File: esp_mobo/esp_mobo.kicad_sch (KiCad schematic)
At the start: 4 parts, among them J1 JST XH Power in, U1 ESP32-DevKitC, U2 74AHCT125

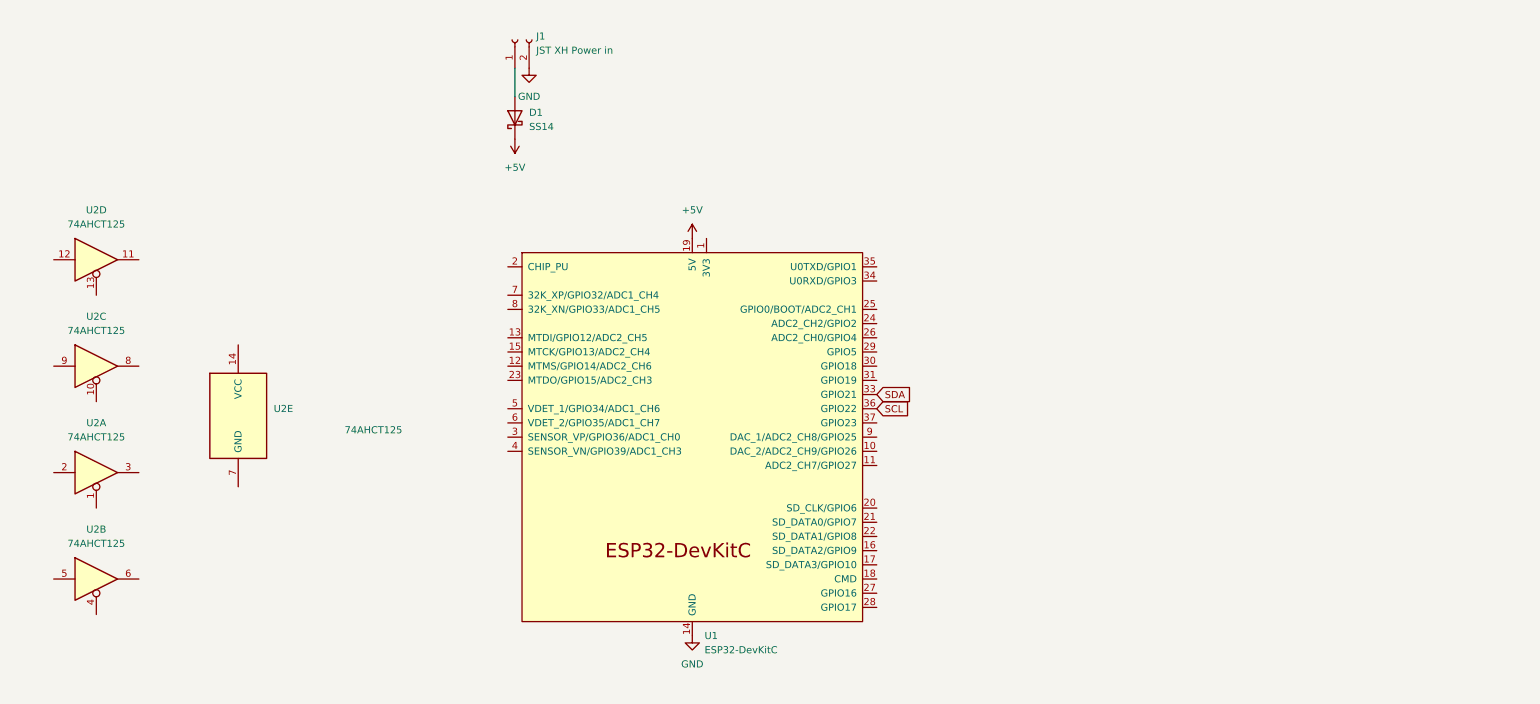
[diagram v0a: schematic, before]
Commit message: add submodule for testing
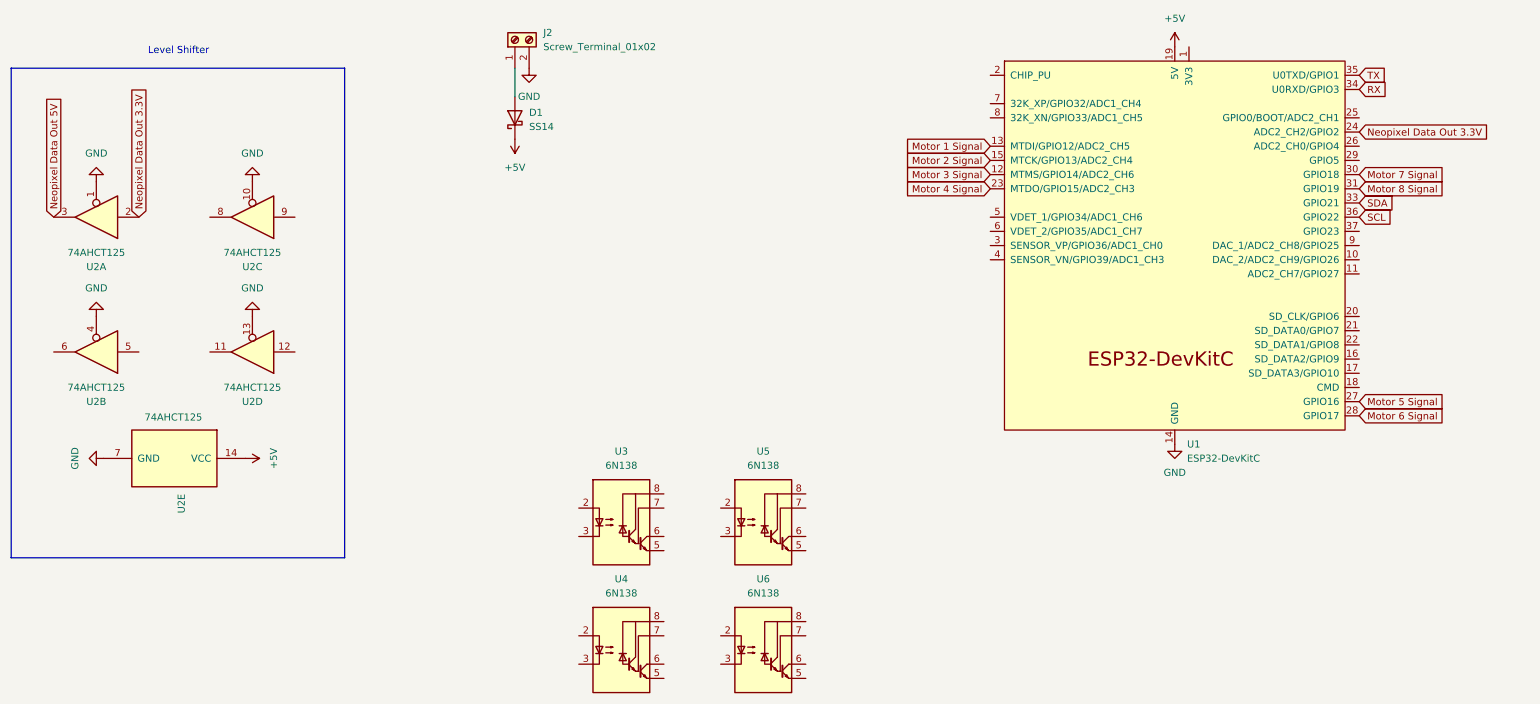
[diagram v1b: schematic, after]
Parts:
- removed J1: JST XH Power in, Connector_JST:JST_XH_B2B-XH-AM_1x02_P2.50mm_Vertical, symbol Connector:Conn_01x02_Socket
- added J2: Screw_Terminal_01x02, TerminalBlock_TE-Connectivity:TerminalBlock_TE_282834-2_1x02_P2.54mm_Horizontal, symbol Connector:Screw_Terminal_01x02
- added U3, U4, U5, U6: 6N138, symbol Isolator:6N138
- U2: footprint (none) -> Package_DIP:DIP-14_W7.62mm
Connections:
- net +5V: now also U2.14 (VCC)
- net GND: now also U2.1, U2.10, U2.13, U2.4, U2.7 (GND), J2.2 (Pin_2)
- net at D1.2 (A): now also J2.1 (Pin_1)
- net Motor 3 Signal: now reaches U1.12 (MTMS/GPIO14/ADC2_CH6)
- net Motor 1 Signal: now reaches U1.13 (MTDI/GPIO12/ADC2_CH5)
- net Motor 2 Signal: now reaches U1.15 (MTCK/GPIO13/ADC2_CH4)
- net Motor 4 Signal: now reaches U1.23 (MTDO/GPIO15/ADC2_CH3)
- net Neopixel Data Out 3.3V: now reaches U1.24 (ADC2_CH2/GPIO2)
- net Neopixel Data Out 3.3V: now also U2.2
- net Motor 5 Signal: now reaches U1.27 (GPIO16)
- net Motor 6 Signal: now reaches U1.28 (GPIO17)
- net Motor 7 Signal: now reaches U1.30 (GPIO18)
- net Motor 8 Signal: now reaches U1.31 (GPIO19)
- net RX: now reaches U1.34 (U0RXD/GPIO3)
- net TX: now reaches U1.35 (U0TXD/GPIO1)
- net Neopixel Data Out 5V: now reaches U2.3
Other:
- note added: "Level Shifter"
- moved on the sheet: U1, U2A, U2B, U2C, U2D, U2E

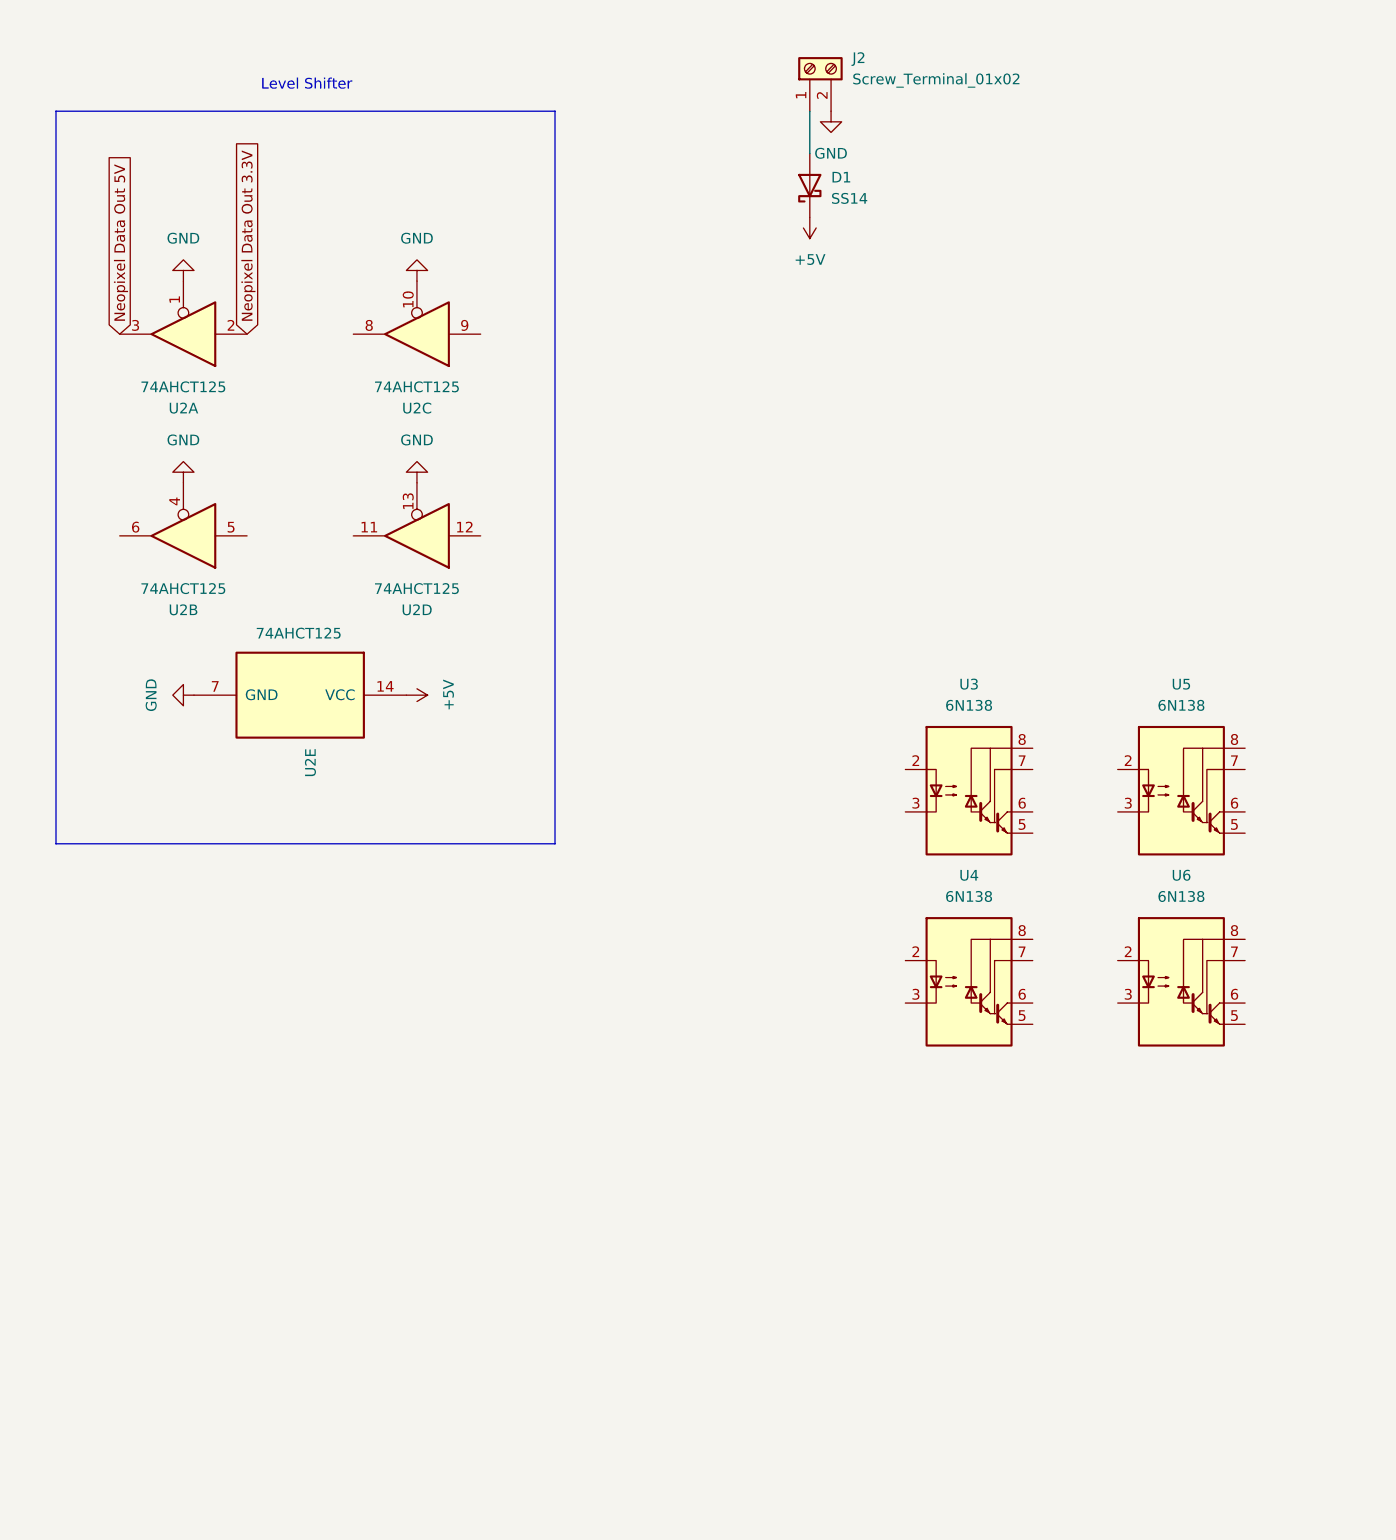
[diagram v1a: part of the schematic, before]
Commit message: Update ESC Mobo with OptoCOuplers and improved circuit
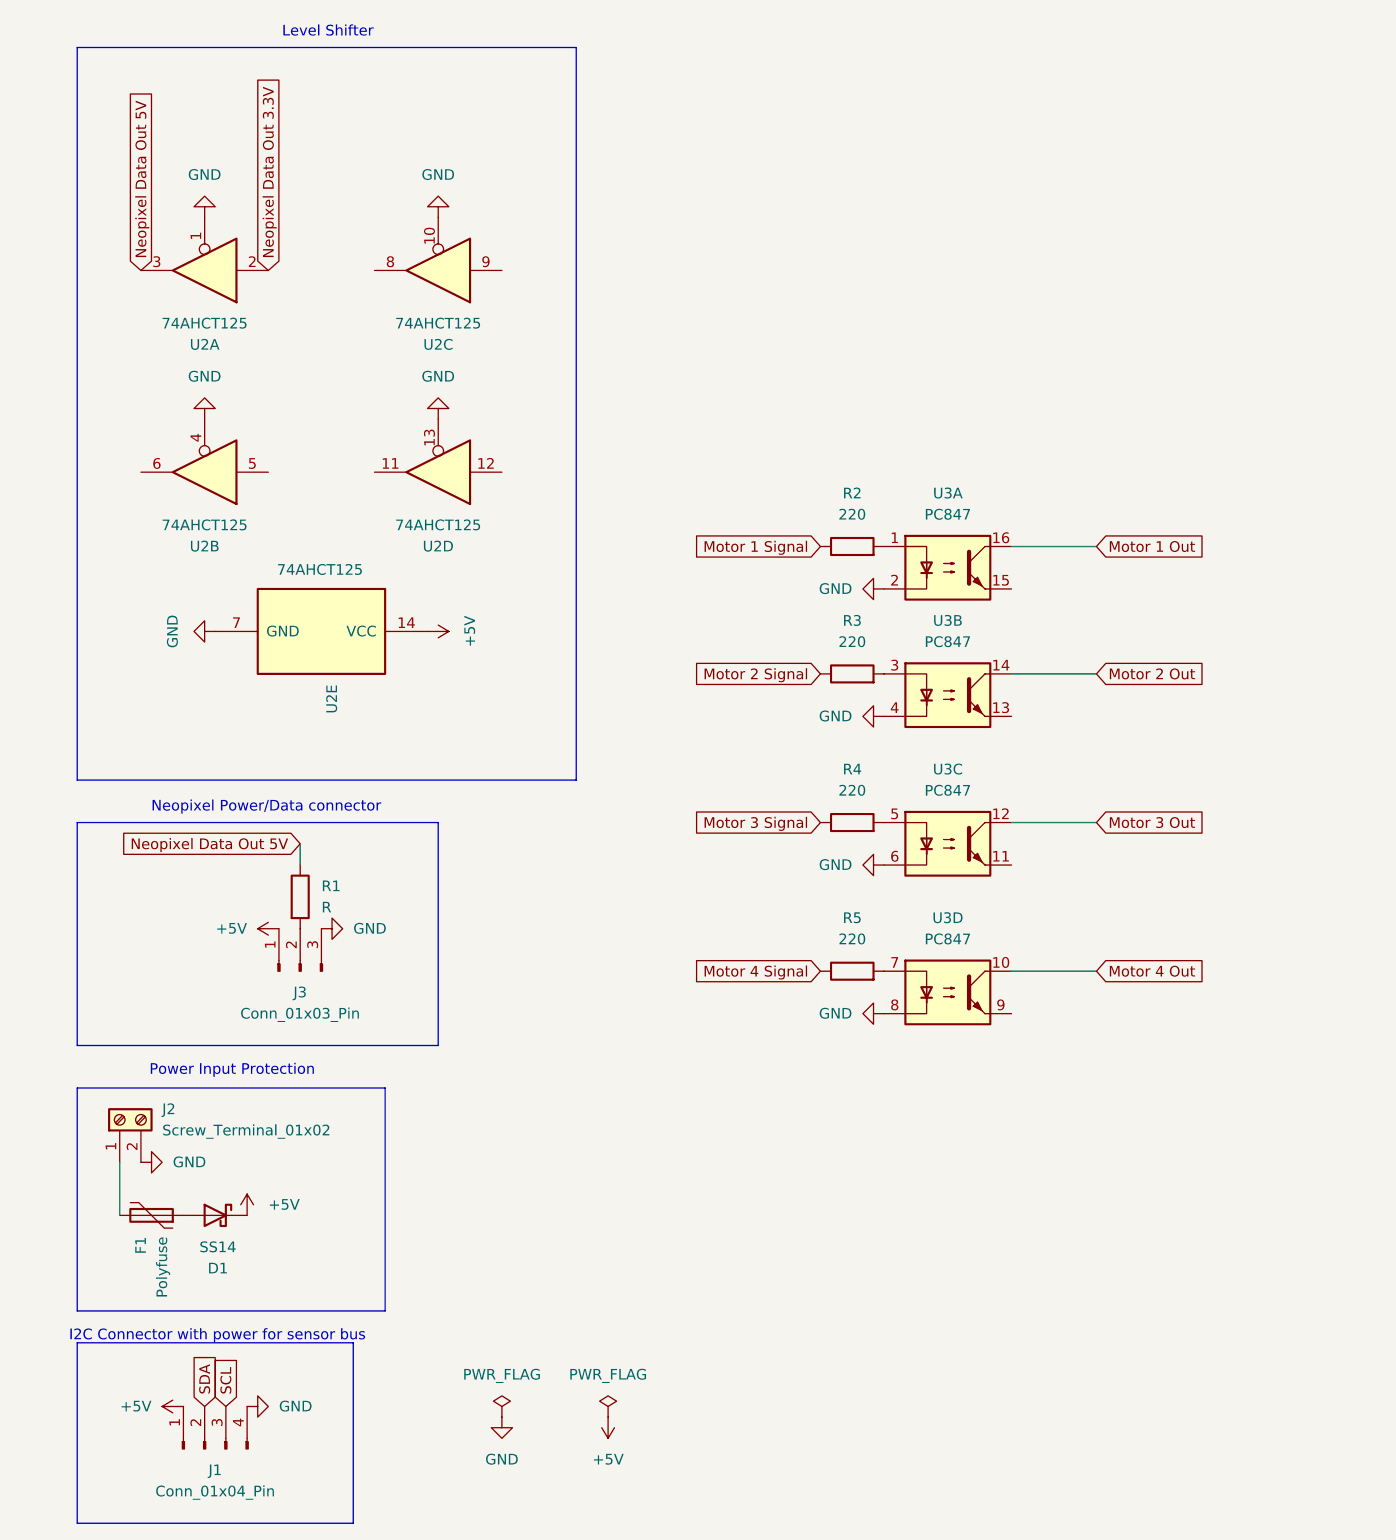
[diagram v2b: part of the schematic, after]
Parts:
- removed U3, U4, U5, U6: 6N138, symbol Isolator:6N138
- added F1: Polyfuse, symbol Device:Polyfuse
- added J1: Conn_01x04_Pin, Connector_JST:JST_XH_B4B-XH-AM_1x04_P2.50mm_Vertical, symbol Connector:Conn_01x04_Pin
- added J3: Conn_01x03_Pin, symbol Connector:Conn_01x03_Pin
- added R1: R, symbol Device:R
- added R2, R3, R4, R5: 220, Resistor_SMD:R_0603_1608Metric_Pad0.98x0.95mm_HandSolder, symbol Device:R
- added U3: PC847, Package_DIP:DIP-16_W7.62mm, symbol Isolator:PC847
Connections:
- net +5V: now also J1.1 (Pin_1), J3.1 (Pin_1)
- net GND: now also J1.4 (Pin_4), J3.3 (Pin_3), U3.2, U3.4, U3.6, U3.8
- net Motor 1 Signal: now also R2.1
- net Motor 2 Signal: now also R3.1
- net Motor 3 Signal: now also R4.1
- net Motor 4 Signal: now also R5.1
- net Neopixel Data Out 5V: now also R1.1
- net SCL: now also J1.3 (Pin_3)
- net SDA: now also J1.2 (Pin_2)
- net at J2.1 (Pin_1): now also F1.2; no longer D1.2 (A)
- new net: J3.2 (Pin_2), R1.2
- new net: R2.2, U3.1
- new net: D1.2 (A), F1.1
- new net: R3.2, U3.3
- new net: R5.2, U3.7
- new net: R4.2, U3.5
- new net Motor 1 Out: U3.16
- new net Motor 2 Out: U3.14
- new net Motor 3 Out: U3.12
- new net Motor 4 Out: U3.10
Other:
- note added: "I2C Connector with power for sensor bus"
- note added: "Neopixel Power/Data connector"
- note added: "Power Input Protection"
- moved on the sheet: D1, J2, U2A, U2B, U2C, U2D, U2E

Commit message: Update ESC Mobo with comments and input protection as well as motor i2c
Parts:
- added C1: C_Polarized, symbol Device:C_Polarized
- added J4: Conn_01x03_Pin, symbol Connector:Conn_01x03_Pin
- added R10, R11, R12, R13: 220, Resistor_SMD:R_0603_1608Metric_Pad0.98x0.95mm_HandSolder, symbol Device:R
- added R14, R15, R16, R17, R6, R7, R8, R9: 220, symbol Device:R
- added U4: PC847, Package_DIP:DIP-16_W7.62mm, symbol Isolator:PC847
- R1: value R -> 220; footprint (none) -> Resistor_SMD:R_0805_2012Metric_Pad1.20x1.40mm_HandSolder
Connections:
- net +5V: now also F1.2, C1.1
- net GND: now also D1.2 (A), C1.2, J4.3 (Pin_3), U4.2, U4.4, U4.6, U4.8
- net Motor 1 Out: now also R6.2
- net Motor 2 Out: now also R7.2
- net Motor 3 Out: now also R8.2
- net Motor 4 Out: now also R9.2
- net Motor 5 Signal: now also R10.1
- net Motor 6 Signal: now also R11.1
- net Motor 7 Signal: now also J4.1 (Pin_1), R12.1
- net Motor 8 Signal: now also J4.2 (Pin_2), R13.1
- net GNDPWR: now reaches U3.15
- net GNDPWR: now also U3.11, U3.13, U3.9, U4.11, U4.13, U4.15, U4.9
- net at J2.1 (Pin_1): now also F1.1; no longer F1.2
- new net: R12.2, U4.5
- new net: R10.2, U4.1
- new net: R11.2, U4.3
- new net: R13.2, U4.7
- new net Motor 5 Out: R14.2, U4.16
- new net Motor 6 Out: R15.2, U4.14
- new net Motor 7 Out: R16.2, U4.12
- new net Motor 8 Out: R17.2, U4.10
- new net Vdrive: R14.1, R15.1, R16.1, R17.1, R6.1, R7.1, R8.1, R9.1
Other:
- note added: "I2C Connector & power sensor bus"
- note added: "I2C Connector for motors"
- note added: "Optoisolators for Motor ESCs"
- note added: "Used as backup for PWM"
- note removed: "I2C Connector with power for sensor bus"
- moved on the sheet: D1, F1, J2, J3, R1, R2, R3, R4, R5, U1, U3A, U3B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

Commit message: Update ESC Mobo
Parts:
- added J5, J6, J7: Conn_01x03_Pin, Connector_PinHeader_2.54mm:PinHeader_1x03_P2.54mm_Vertical, symbol Connector:Conn_01x03_Pin
- F1: footprint (none) -> Fuse:Fuse_Bourns_MF-RG300
- J3, J4: footprint (none) -> Connector_JST:JST_XH_B3B-XH-AM_1x03_P2.50mm_Vertical
- R14, R15, R16, R17, R6, R7, R8, R9: footprint (none) -> Resistor_SMD:R_0603_1608Metric_Pad0.98x0.95mm_HandSolder
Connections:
- net +5V: now also J5.1 (Pin_1), J5.2 (Pin_2), J5.3 (Pin_3)
- net GND: now also J7.1 (Pin_1), J7.2 (Pin_2), J7.3 (Pin_3)
- net Servo2 Data Out: now reaches U2.8
- net Servo2 Data Out: now also J6.2 (Pin_2)
- net Servo2 Data In: now reaches U2.9
- net Servo2 Data In: now also U1.7 (32K_XP/GPIO32/ADC1_CH4)
- net Servo3 Data Out: now reaches U2.11
- net Servo3 Data Out: now also J6.3 (Pin_3)
- net Servo3 Data In: now reaches U2.12
- net Servo3 Data In: now also U1.8 (32K_XN/GPIO33/ADC1_CH5)
- net Servo1 Data In: now reaches U1.26 (ADC2_CH0/GPIO4)
- net Servo1 Data In: now also U2.5
- net Servo1 Data Out: now reaches U2.6
- net Servo1 Data Out: now also J6.1 (Pin_1)
- no-connect marks 0 -> 5
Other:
- note added: "Servo Ports"
- moved on the sheet: C1, D1, F1, J2

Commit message: Update ESC Mobo
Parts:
- added C2, C3, C4, C5: 100uf, Capacitor_SMD:C_0603_1608Metric, symbol Device:C
- added C6, C7: 100nF, symbol Device:C
- added D2, D3, D4, D5: WS2812B, LED_SMD:LED_WS2812B_PLCC4_5.0x5.0mm_P3.2mm, symbol LED:WS2812B
- added H1, H2, H3, H4: MountingHole_Pad, MountingHole:MountingHole_3.2mm_M3_Pad, symbol Mechanical:MountingHole_Pad
- added J10, J11, J12, J13, J14, J15, J8, J9: Conn_01x03_Pin, Connector_PinHeader_2.54mm:PinHeader_1x03_P2.54mm_Vertical, symbol Connector:Conn_01x03_Pin
- added J16: Conn_01x02_Pin, Connector_PinHeader_2.54mm:PinHeader_1x02_P2.54mm_Vertical, symbol Connector:Conn_01x02_Pin
- added JP1: Jumper_2_Open, Connector_PinHeader_2.54mm:PinHeader_1x02_P2.54mm_Vertical, symbol Jumper:Jumper_2_Open
- added JP2: Jumper_2_Open, symbol Jumper:Jumper_2_Open
- added R18, R19: 4.7K, symbol Device:R
- added U5: BME280, Package_LGA:Bosch_LGA-8_2.5x2.5mm_P0.65mm_ClockwisePinNumbering, symbol Sensor:BME280
- C1: footprint (none) -> Capacitor_THT:CP_Radial_D5.0mm_P2.00mm
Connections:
- net +5V: now also C2.2, C3.2, C4.2, C5.2, D2.1 (VDD), D3.1 (VDD), D4.1 (VDD), D5.1 (VDD), J16.1 (Pin_1)
- net GND: now also C2.1, C3.1, C4.1, C5.1, C6.2, C7.1, D2.3 (VSS), D3.3 (VSS), D4.3 (VSS), D5.3 (VSS), H1.1, H2.1, H3.1, H4.1, JP2.2 (B), U5.1 (GND), U5.7 (GND)
- net GNDPWR: now also J10.3 (Pin_3), J11.3 (Pin_3), J12.3 (Pin_3), J13.3 (Pin_3), J14.3 (Pin_3), J15.3 (Pin_3), J8.3 (Pin_3), J9.3 (Pin_3)
- net Motor 1 Out: now also J8.1 (Pin_1)
- net Motor 2 Out: now also J9.1 (Pin_1)
- net Motor 3 Out: now also J10.1 (Pin_1)
- net Motor 4 Out: now also J11.1 (Pin_1)
- net Motor 5 Out: now also J12.1 (Pin_1)
- net Motor 6 Out: now also J13.1 (Pin_1)
- net Motor 7 Out: now also J14.1 (Pin_1)
- net Motor 8 Out: now also J15.1 (Pin_1)
- net Neopixel Data Out 5V: now also D5.2 (DOUT); no longer U2.3
- net Vdrive: now also J10.2 (Pin_2), J11.2 (Pin_2), J12.2 (Pin_2), J13.2 (Pin_2), J14.2 (Pin_2), J15.2 (Pin_2), J16.2 (Pin_2), J8.2 (Pin_2), J9.2 (Pin_2)
- net +3.3V: now reaches U1.1 (3V3)
- net +3.3V: now also C6.1, C7.2, JP1.2 (B), R18.1, R19.1, U5.2 (CSB), U5.6 (VDDIO), U5.8 (VDD)
- new net: JP1.1 (A), JP2.1 (A), U5.5 (SDO)
- new net: D3.2 (DOUT), D4.4 (DIN)
- new net: D2.2 (DOUT), D3.4 (DIN)
- new net: R19.2, U5.4 (SCK)
- new net: R18.2, U5.3 (SDI)
- new net: D4.2 (DOUT), D5.4 (DIN)
- new net NeoPixel Onboard: D2.4 (DIN), U2.3
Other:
- note added: "Built in LEDs"
- note added: "Optocoupler Bypass Decoupling for motors with no UBEC"
- note added: "PWM Motor Connectors"
